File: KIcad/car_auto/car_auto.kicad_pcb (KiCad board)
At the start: 2 copper layers, 96 x 96 mm, 26 parts, among them J1 PONTE-H, J2 HMC5883L, J3 NEO-6M, J4 ALIMENTAÇÃO, U1 ESP32-DEVKITC-32D, U2 ZC142200

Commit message: feat: Implementação da classe para controle dos motores via Bluetooth.
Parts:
- removed the ? at (112.5, 79.5)
- removed the ? at (97.5, 70.0)
- removed the ? at (93.5, 70.0)
- removed the ? at (107.5, 79.5)
- removed J3: NEO-6M, importados:JST_B4P-VH_LF__SN_
- removed U2: ZC142200, importados:MODULE_ZC142200
- added ?: , , F.Cu at (125.6, 107.1)
- added ?: , , F.Cu at (125.6, 87.7)
- added R1: 1.8k, Resistor_THT:R_Axial_DIN0207_L6.3mm_D2.5mm_P10.16mm_Horizontal, F.Cu at (125.6, 82.9)
- added R2: 3.3k, Resistor_THT:R_Axial_DIN0207_L6.3mm_D2.5mm_P10.16mm_Horizontal, F.Cu at (132.3, 82.9)
- added SW1: MTS-102, importados:MTS-102, F.Cu at (129.5, 59.6)
- added U3: ~, importados:NEO-6M-V2-GPSMODULE-FOOTPRINT, F.Cu at (154.9, 84.4)
- moved ? 9.06 mm to (106.4, 124.0)
- moved ? 9.06 mm to (106.4, 129.0)
- moved ? 9.06 mm to (106.4, 126.5)
- moved ? 9.06 mm to (106.4, 131.5)
- moved ? 9.06 mm to (106.4, 121.5)
- moved ? 9.06 mm to (106.4, 119.0)
- moved U1 9.06 mm to (104.4, 109.0)
- moved ? 8.50 mm to (146.5, 119.0)
- moved ? 8.50 mm to (146.5, 131.5)
- moved ? 8.50 mm to (146.5, 126.5)
- moved ? 8.50 mm to (146.5, 121.5)
- moved ? 8.50 mm to (146.5, 129.0)
- moved ? 8.50 mm to (146.5, 124.0)
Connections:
- U1 pad J3-2: unconnected-(U1-IO23-PadJ3-2) -> enable
- U1 pad J3-8: unconnected-(U1-IO19-PadJ3-8) -> sinal_controle
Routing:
- net TX-HC_05: track 63.6 -> 0.00 mm
- net RX-HC_05: track 47.6 -> 0.00 mm
- net GND: track 227.8 -> 251.8 mm
- net sinal_controle: track 0.00 -> 20.1 mm
- net Net-(R1-Pad2): track 0.00 -> 15.3 mm
- net SDA: track 42.2 -> 52.7 mm
- net SCL: track 36.3 -> 46.0 mm
- net PMW-A: track 50.4 -> 41.9 mm
- net IN3-B: track 48.1 -> 40.1 mm
- net PMW-B: track 50.0 -> 42.0 mm
- net IN4-B: track 47.5 -> 39.8 mm
- net IN1-A: track 49.1 -> 42.0 mm
- net IN2-A: track 48.5 -> 41.4 mm
- net VCC: track 256.8 -> 263.1 mm
- net GPS-RX: track 49.1 -> 42.8 mm
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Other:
- outline, holes or cut-outs redrawn

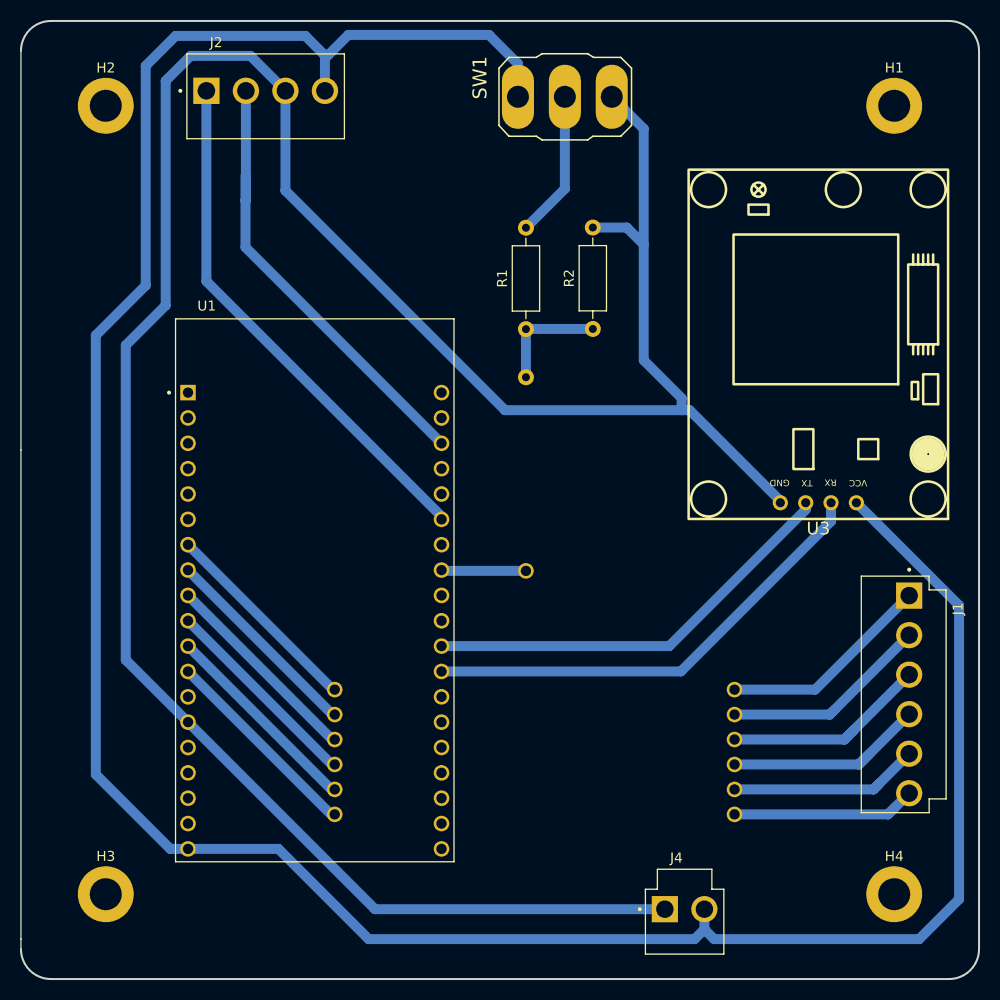
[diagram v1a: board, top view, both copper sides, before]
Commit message: feat: Implement navigation system with compass and motor control
- Added Bussola class for compass handling with filtering.
- Introduced Motor class for H-bridge motor control with PWM support.
- Created Navigator class to manage robot navigation and movement towards targets.
- Implemented GPS functionality for location tracking and filtering.
- Updated main loop to integrate navigation and movement logic.
- Refactored control_motor methods to use PWM for speed control.
- Added Kalman filter for improved sensor data processing.
- Enhanced remote control functionality for directional movement.
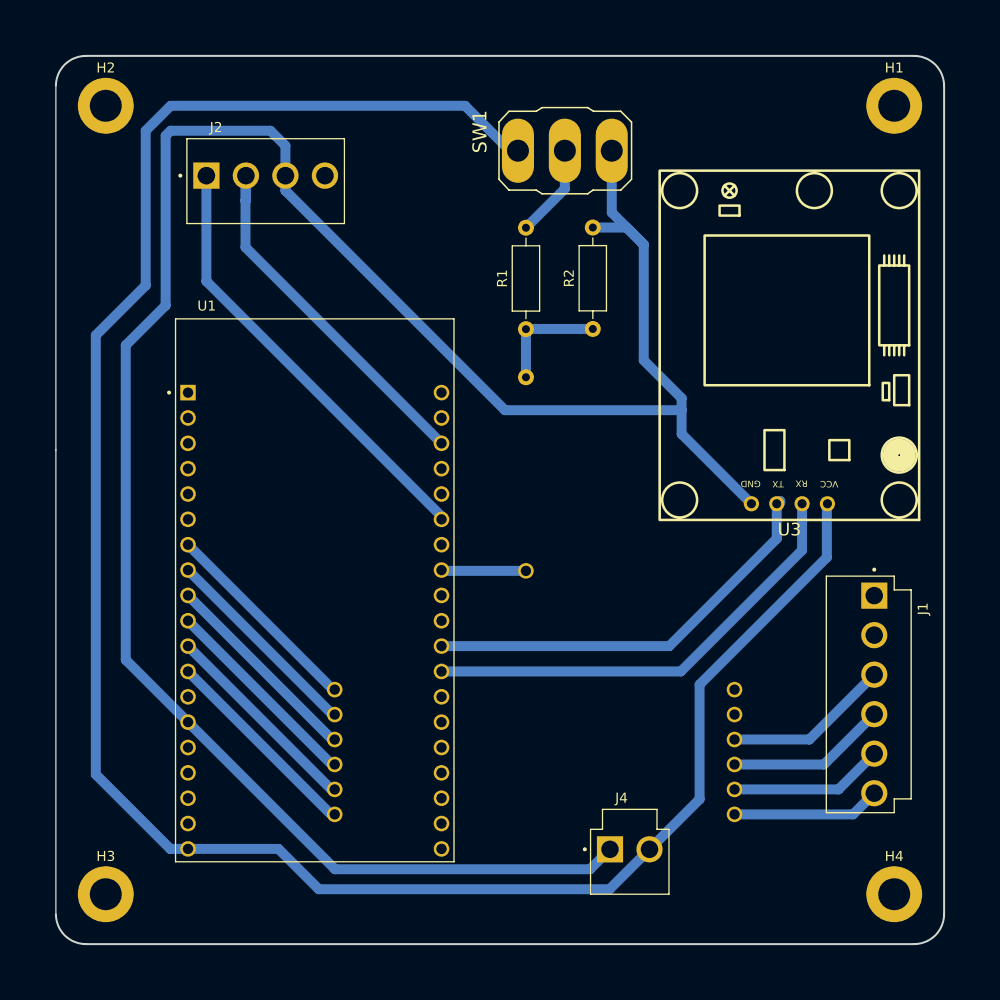
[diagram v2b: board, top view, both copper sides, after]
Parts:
- moved J2 8.50 mm to (99.5, 67.5)
- moved J4 8.14 mm to (136.0, 135.0)
- moved SW1 5.40 mm to (129.5, 65.0)
- moved J1 3.50 mm to (160.5, 119.5)
- moved U3 2.90 mm to (152.0, 84.5)
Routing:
- net VCC: track 263.1 -> 210.7 mm
- net GND: track 251.8 -> 224.3 mm
- net PMW-B: track 42.0 -> 20.5 mm
- net PMW-A: track 41.9 -> 20.5 mm
- net SDA: track 52.7 -> 44.2 mm
- net SCL: track 46.0 -> 37.5 mm
- net Net-(R1-Pad2): track 15.3 -> 9.34 mm
- net IN2-A: track 41.4 -> 36.5 mm
- net IN1-A: track 42.0 -> 37.1 mm
- net IN4-B: track 39.8 -> 35.1 mm
- net IN3-B: track 40.1 -> 35.8 mm
- net GPS-TX: track 47.1 -> 45.8 mm
- net GPS-RX: track 42.8 -> 41.7 mm
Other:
- board size 96 x 96 mm -> 89 x 89 mm
